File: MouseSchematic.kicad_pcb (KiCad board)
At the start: 2 copper layers, 67 parts, among them IC1 AZ1117IH-3.3TRG1, J1 Right Header, J2 Right Header, J4 JST1, J5 JST2, J6 Programming Header, Q1 IR Receiver, Q2 IR Receiver, Q3 IR Receiver, Q4 IR Receiver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

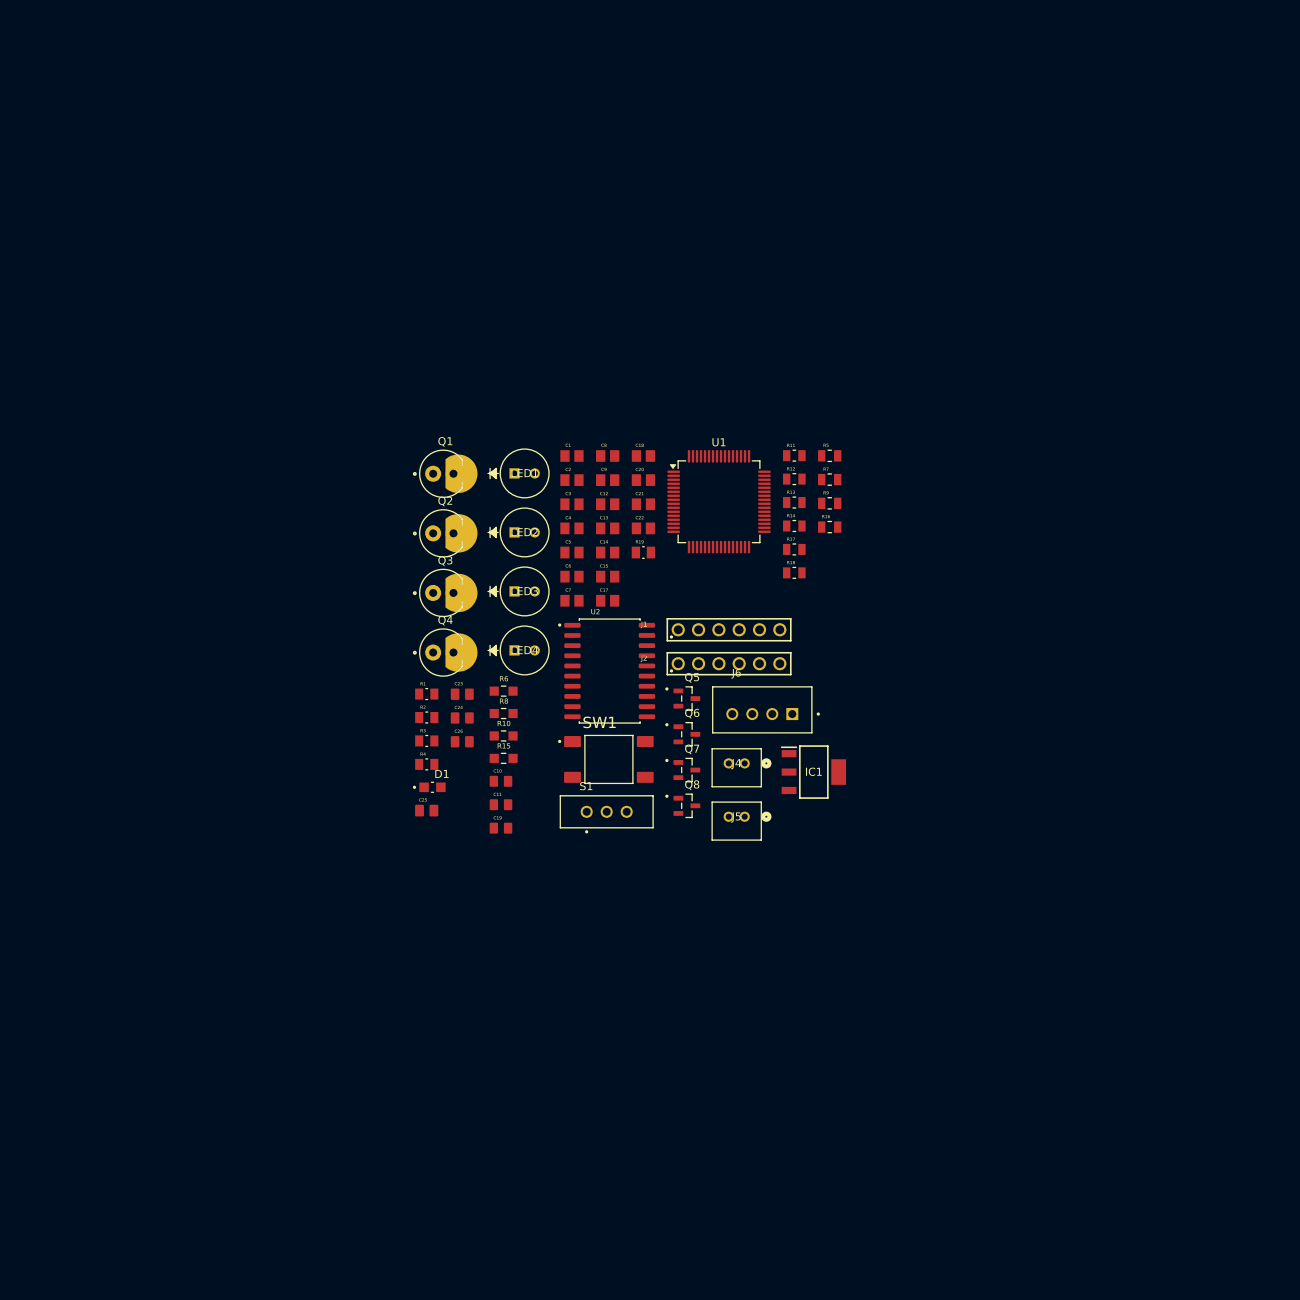
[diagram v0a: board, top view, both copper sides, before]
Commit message: Started layout (laid out 1 IR sensor/emitter pair, motor driver, and put components in general location)
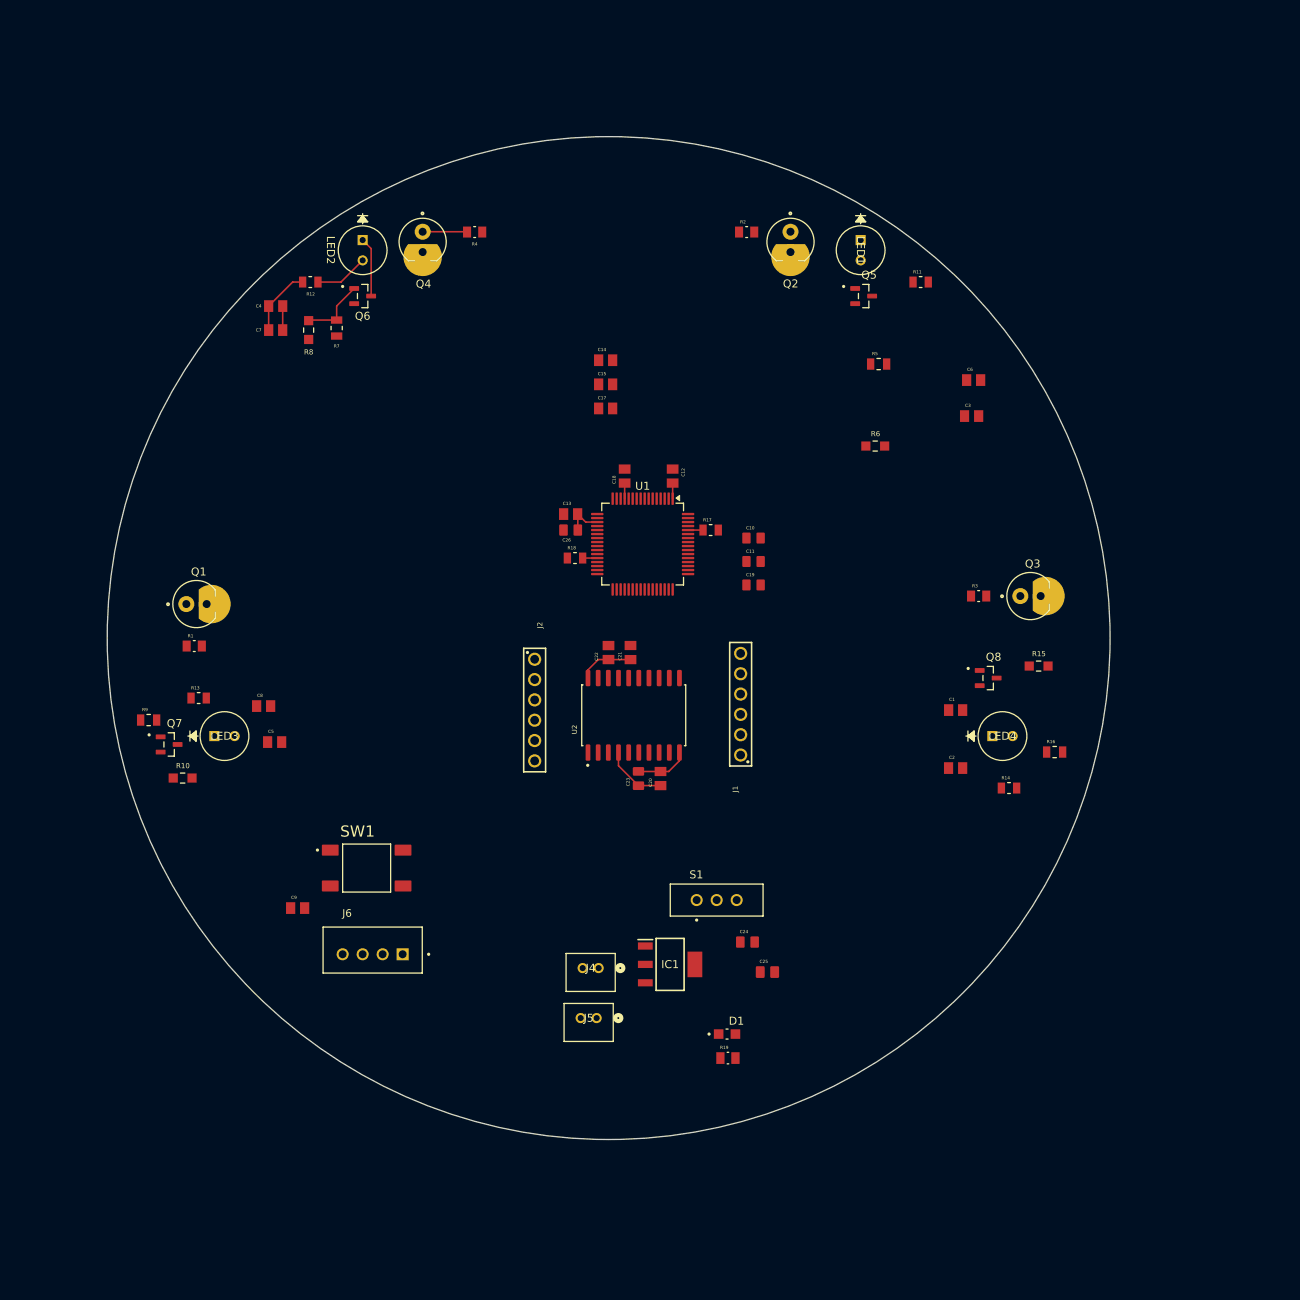
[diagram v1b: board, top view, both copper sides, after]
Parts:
- J2: value Right Header -> Left Header
- moved R9 89.3 mm to (94.8, 114.0)
- moved R13 78.4 mm to (101.0, 111.2)
- moved Q3 73.4 mm to (205.0, 98.5)
- moved R2 72.7 mm to (169.5, 53.0)
- moved R3 71.3 mm to (198.5, 98.5)
- moved Q6 68.1 mm to (121.5, 61.0)
- moved R15 67.9 mm to (206.0, 107.2)
- moved R4 66.8 mm to (135.5, 53.0), turned to 180 degrees
- moved C9 66.1 mm to (113.4, 137.5)
- moved R12 65.3 mm to (115.0, 59.2), turned to 180 degrees
- moved Q7 64.8 mm to (97.3, 117.0)
- moved R7 64.5 mm to (118.2, 65.0), turned to -90 degrees
- moved R19 64.1 mm to (167.2, 156.2)
- moved LED4 60.7 mm to (200.2, 116.0)
- moved C2 60.0 mm to (195.6, 120.0)
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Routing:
- net 3V3: track 0.00 -> 17.3 mm
- net VCC: track 0.00 -> 13.6 mm
- net GND: track 0.00 -> 10.9 mm
- net Net-(Q6-Pad1): track 0.00 -> 8.39 mm
- net Net-(LED2-Pad1): track 0.00 -> 7.44 mm
- net Net-(LED2-Pad2): track 0.00 -> 6.71 mm
- net PA6: track 0.00 -> 5.57 mm
- net Net-(U1-BOOT0): track 0.00 -> 1.87 mm
- net Net-(U1-PB2): track 0.00 -> 1.82 mm
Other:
- board outline added: 125.4 x 125.4 mm

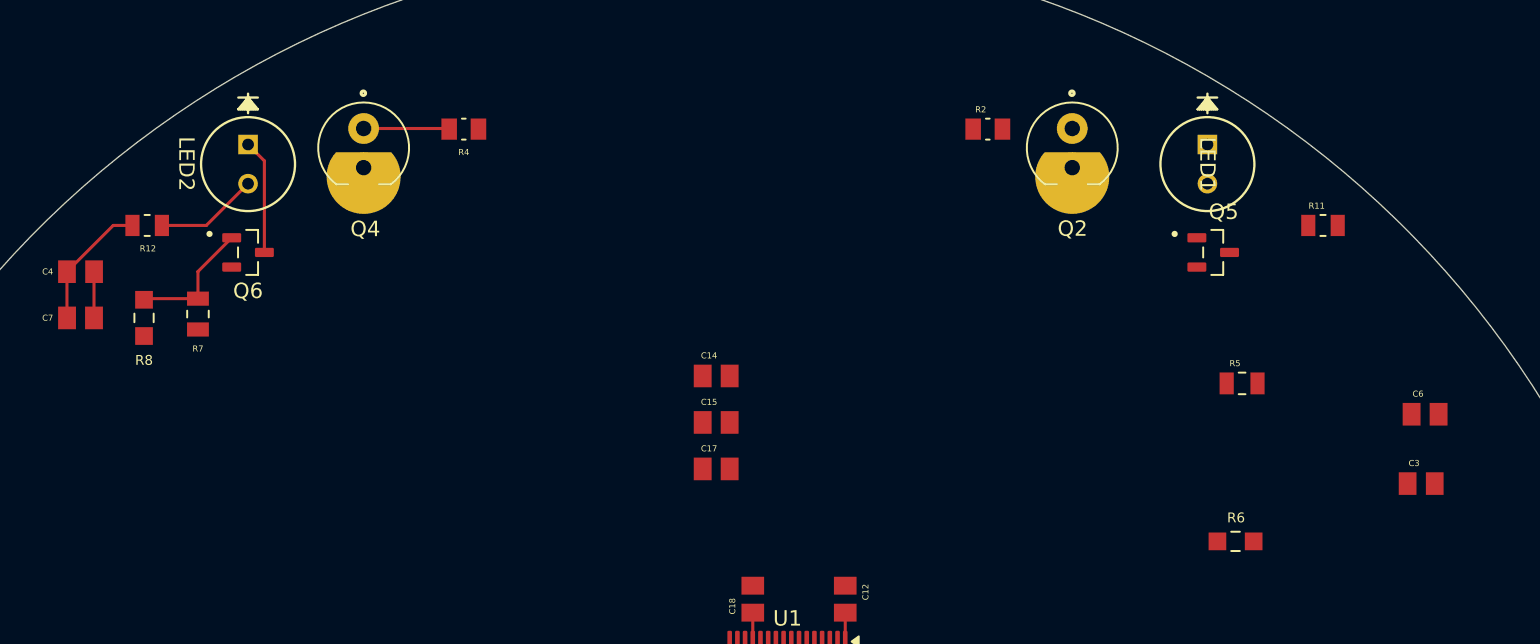
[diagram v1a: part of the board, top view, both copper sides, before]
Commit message: Added 2nd IR sensor emitter pair
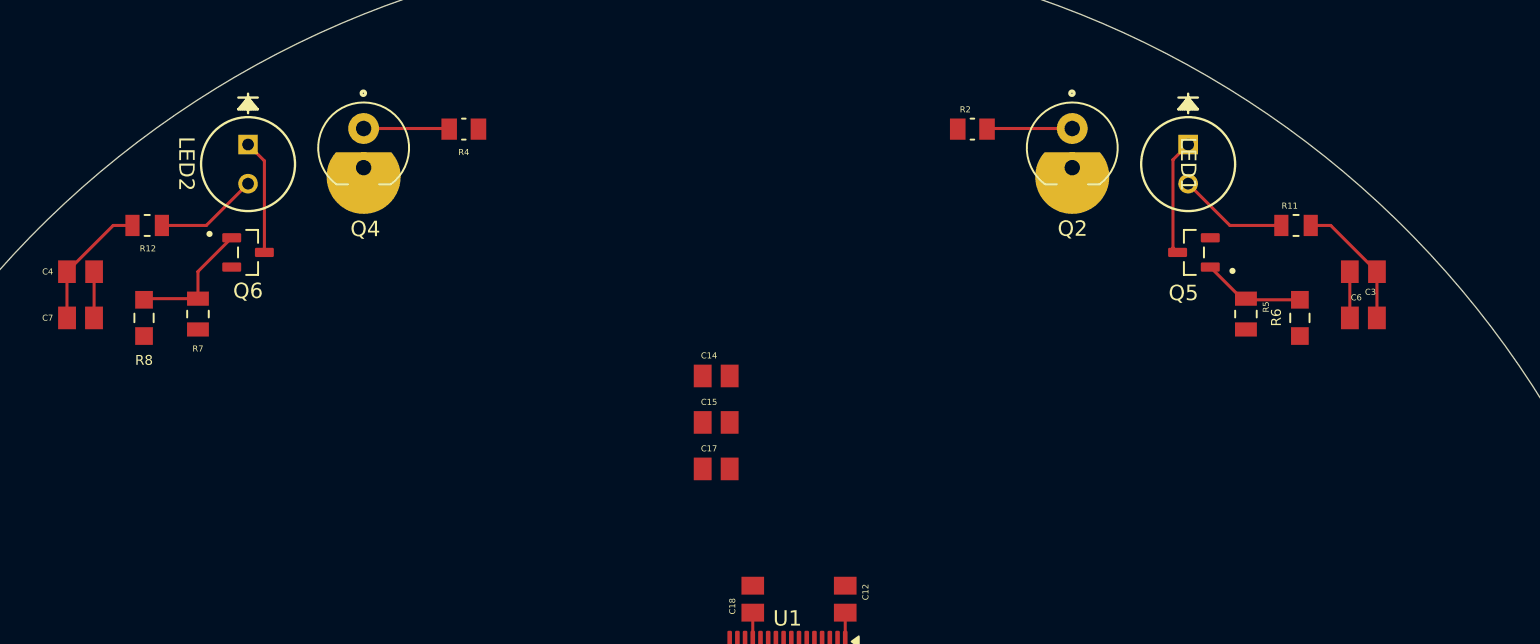
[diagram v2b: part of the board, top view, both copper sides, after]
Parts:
- moved R6 15.1 mm to (189.8, 65.2), turned to 90 degrees
- moved C3 14.3 mm to (193.9, 62.2), turned to 180 degrees
- moved C6 7.42 mm to (193.9, 65.2)
- moved R5 4.51 mm to (186.2, 65.0), turned to -90 degrees
- moved R11 1.75 mm to (189.5, 59.2)
- moved LED1 1.25 mm to (182.5, 54.0)
- moved Q5 1.25 mm to (182.9, 61.0), turned to 180 degrees
- moved R2 1.00 mm to (168.5, 53.0)
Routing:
- net 3V3: track 17.3 -> 25.8 mm
- net Net-(LED1-Pad1): track 0.00 -> 7.53 mm
- net Net-(LED1-Pad2): track 0.00 -> 7.17 mm
- net Net-(Q5-Pad1): track 0.00 -> 6.70 mm
- net PB1: track 0.00 -> 5.55 mm
- net GND: track 10.9 -> 13.9 mm

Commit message: Finished main layout of components still need to finish final touches and traces
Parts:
- moved R10 49.4 mm to (141.2, 95.5), turned to -90 degrees
- moved R9 47.8 mm to (138.9, 95.8), turned to 90 degrees
- moved Q7 44.1 mm to (137.9, 99.8), turned to -90 degrees
- moved R13 42.7 mm to (142.2, 100.3)
- moved C8 39.9 mm to (144.6, 94.0)
- moved C5 39.4 mm to (144.6, 97.0), turned to 180 degrees
- moved R16 37.6 mm to (177.7, 95.7), turned to -90 degrees
- moved R14 36.5 mm to (173.7, 99.8), turned to 180 degrees
- moved R1 34.8 mm to (129.7, 85.8), turned to -90 degrees
- moved R15 33.0 mm to (175.2, 95.4), turned to -90 degrees
- moved C2 32.9 mm to (172.4, 96.8)
- moved LED3 32.2 mm to (130.8, 99.8)
- moved Q1 31.1 mm to (130.9, 92.3)
- moved C1 30.0 mm to (172.4, 93.8), turned to 180 degrees
- moved C9 29.1 mm to (139.1, 124.0)
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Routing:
- net 3V3: track 25.8 -> 61.8 mm
- net NRST: track 0.00 -> 12.4 mm
- net GND: track 13.9 -> 22.4 mm
- net Net-(LED3-Pad2): track 0.00 -> 8.17 mm
- net Net-(LED3-Pad1): track 0.00 -> 7.62 mm
- net Net-(LED4-Pad1): track 0.00 -> 7.59 mm
- net Net-(J4-Pad2): track 0.00 -> 7.25 mm
- net Net-(LED4-Pad2): track 0.00 -> 7.07 mm
- net PC4: track 0.00 -> 5.81 mm
- net PC5: track 0.00 -> 5.56 mm
- net Net-(Q8-Pad1): track 0.00 -> 4.87 mm
- net Net-(Q7-Pad1): track 0.00 -> 4.28 mm
- net Net-(D1-Pad1): track 0.00 -> 2.82 mm
- net Net-(IC1-INPUT): track 0.00 -> 2.25 mm
- net Net-(U1-VCAP_2): track 0.00 -> 2.25 mm
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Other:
- board size 125.4 x 125.4 mm -> 88.4 x 88.4 mm

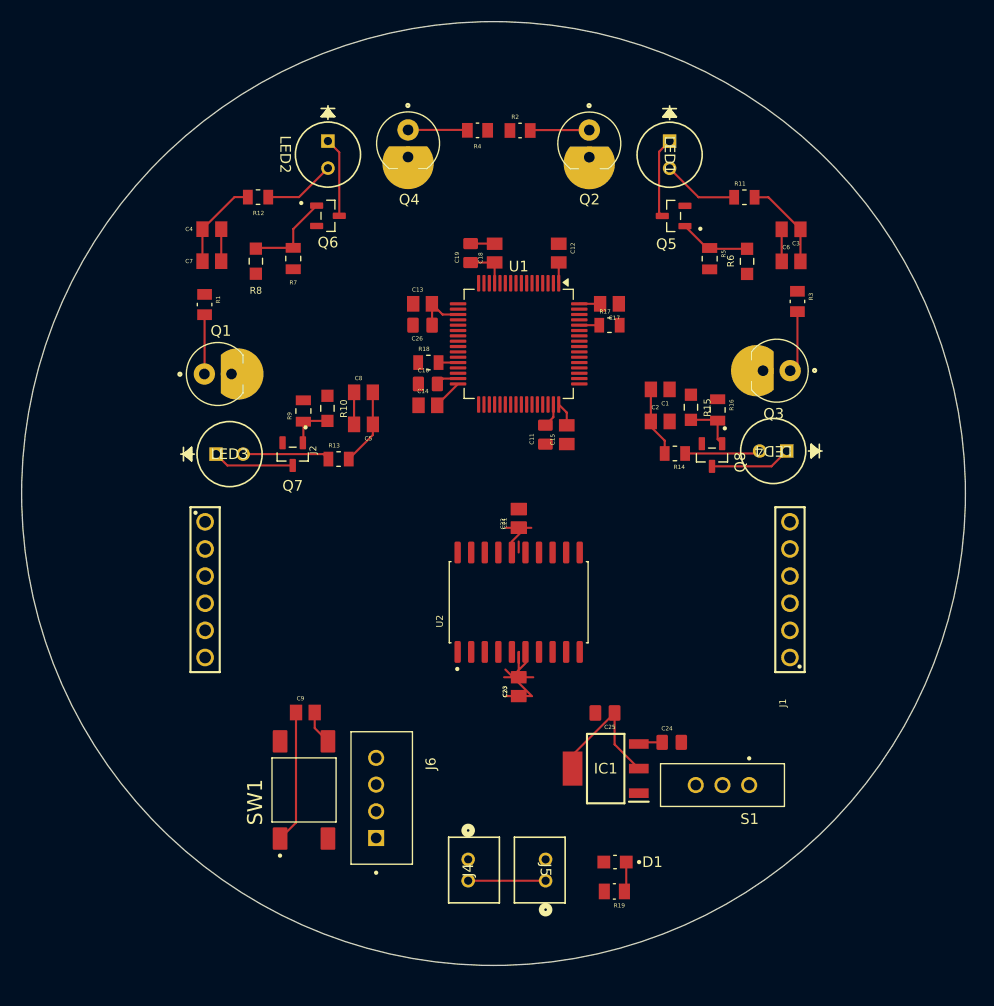
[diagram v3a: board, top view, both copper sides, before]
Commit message: Added traces but now gotta move components a little further apart from each other to make room for fill zones
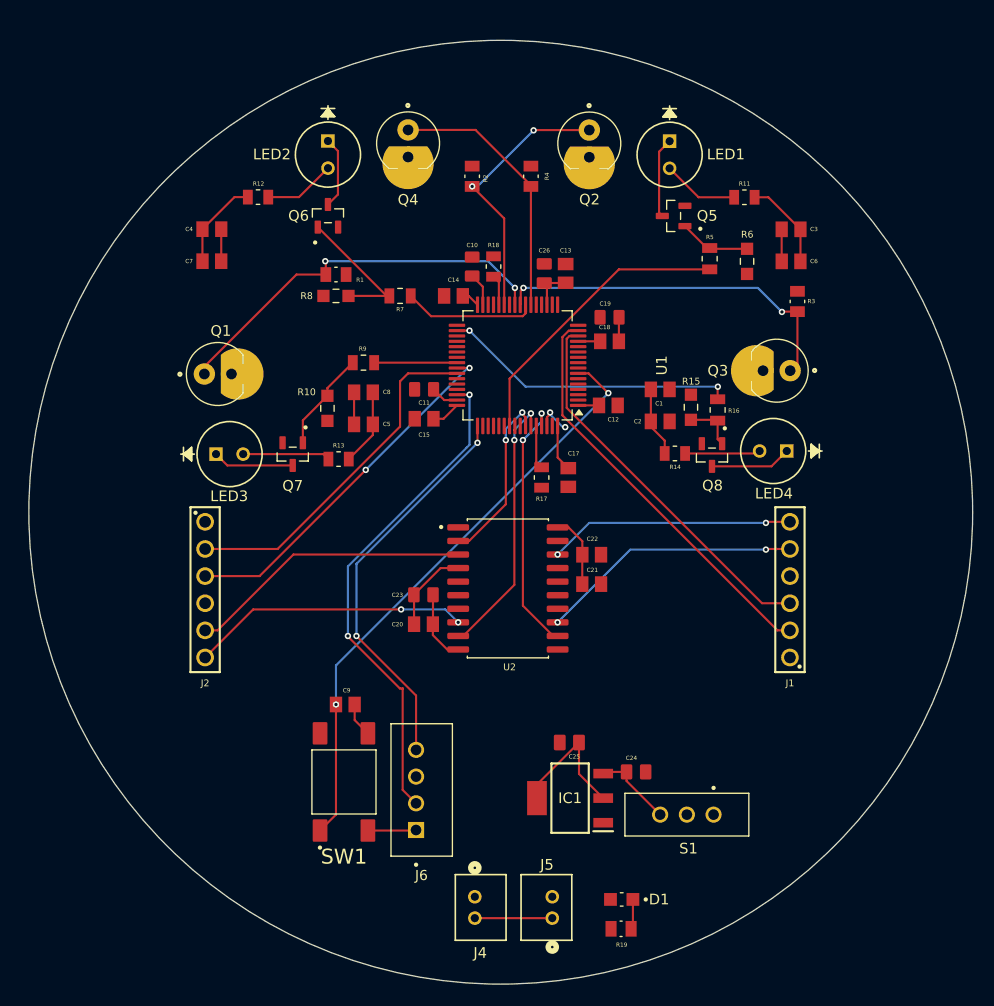
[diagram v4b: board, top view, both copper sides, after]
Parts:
- moved C17 16.7 mm to (163.8, 102.0), turned to 90 degrees
- moved R17 15.6 mm to (161.2, 102.0), turned to -90 degrees
- moved C12 15.0 mm to (167.5, 95.2), turned to 180 degrees
- moved C19 14.3 mm to (167.6, 87.0), turned to 0 degrees
- moved C13 13.7 mm to (163.5, 82.9), turned to -90 degrees
- moved C18 13.6 mm to (167.6, 89.2), turned to 0 degrees
- moved C15 13.4 mm to (150.2, 96.5), turned to 0 degrees
- moved R1 12.6 mm to (142.0, 83.0), turned to 180 degrees
- moved C23 12.4 mm to (150.2, 113.0), turned to 0 degrees
- moved C26 12.4 mm to (161.5, 82.9), turned to -90 degrees
- moved C11 12.1 mm to (150.2, 93.8), turned to 0 degrees
- moved C10 11.7 mm to (154.8, 82.2), turned to -90 degrees
- moved R18 10.9 mm to (156.8, 82.2), turned to -90 degrees
- moved C20 10.7 mm to (150.2, 115.7), turned to 0 degrees
- moved R7 10.6 mm to (148.0, 85.0), turned to 0 degrees
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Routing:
- net PA13: track 0.00 -> 46.9 mm, vias 0 -> 2
- net NRST: track 12.4 -> 55.7 mm, vias 0 -> 2
- net PA1: track 0.00 -> 38.7 mm
- net PA14: track 0.00 -> 37.3 mm, vias 0 -> 2
- net PA0: track 0.00 -> 36.1 mm
- net PA8: track 0.00 -> 34.0 mm, vias 0 -> 2
- net PA9: track 0.00 -> 32.9 mm
- net PC5: track 5.56 -> 37.3 mm, vias 0 -> 2
- net PC4: track 5.81 -> 34.1 mm, vias 0 -> 2
- net PB13: track 0.00 -> 27.8 mm, vias 0 -> 2
- net PB3: track 0.00 -> 27.4 mm
- net ML2: track 0.00 -> 26.6 mm
- net ML1: track 0.00 -> 26.1 mm, vias 0 -> 2
- net PB7: track 0.00 -> 25.1 mm, vias 0 -> 2
- net MR2: track 0.00 -> 24.6 mm, vias 0 -> 2
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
